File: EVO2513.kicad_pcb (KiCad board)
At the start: 8 copper layers, 110 x 69 mm, 272 parts, among them J1 1053101204, J2 1053101114, J3 10144517-043802LF, J4 1053102204, J5 1053091102, J6 1053091102, M1 78614150960, M2 78614150960, M3 78614150960, M4 78614150960, M5 78614150960, M6 78614150960, Q1 DMT6007LFGQ-7, Q10 DMT4011LFG, Q11 DMT4011LFG, Q12 DMP3007SCG-13, Q13 DMP3007SCG-13, Q14 DMP3007SCG-13, Q15 DMP3007SCG-13, Q16 IAUCN04S7L019, Q17 IAUCN04S7L028, Q18 CSD17304Q3, Q19 IAUCN04S7L019, Q20 BSS138, Q21 BSS138, Q22 BSS138, Q23 BSS138, Q24 BSS138, Q3 DMT6007LFGQ-7, Q4 DMP3007SCG-13, Q5 DMP3007SCG-13, Q6 DMT4011LFG, Q7 DMT4011LFG, Q8 DMT4011LFG, Q9 DMT4011LFG, U1 LTC1960, U10 TLV9002IDSG, U11 PCAL9714, U2 LTC4365, U5 LM51772RHAR, U6 TPS22811, U7 TPS22811, U8 TLV9002IDSG, U9 TPS22811

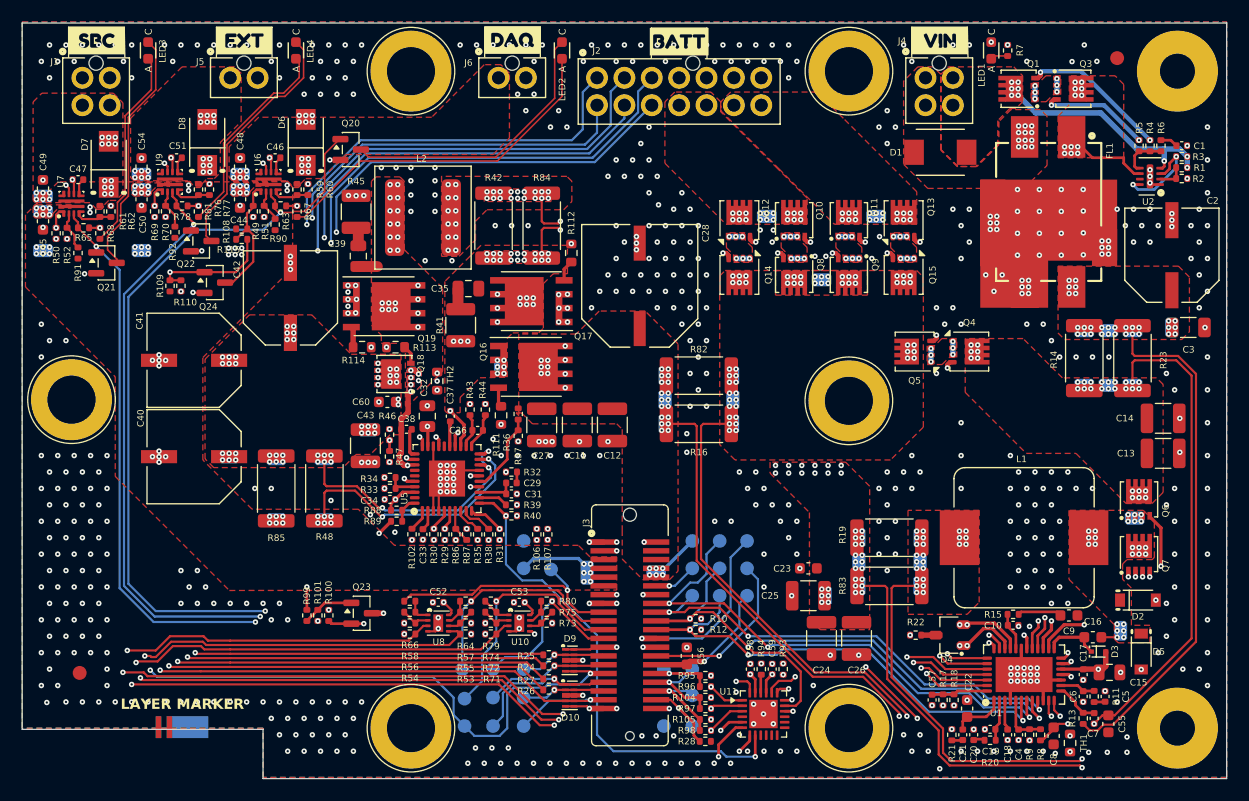
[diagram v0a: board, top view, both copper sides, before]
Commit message: Remove C55; charger layout; QC and S/N boxes
- C55 removed from the schematic and board.
- Charger-area placement and routing around U1 (C8, C7, R13, D3, DCSENSED).
- Filled QC and S/N marking boxes on the front silkscreen.

DRC: 23 violations (silk/text only), 0 unconnected, 0 parity.

Co-Authored-By: Claude Opus 5.5 <noreply@anthropic.com>
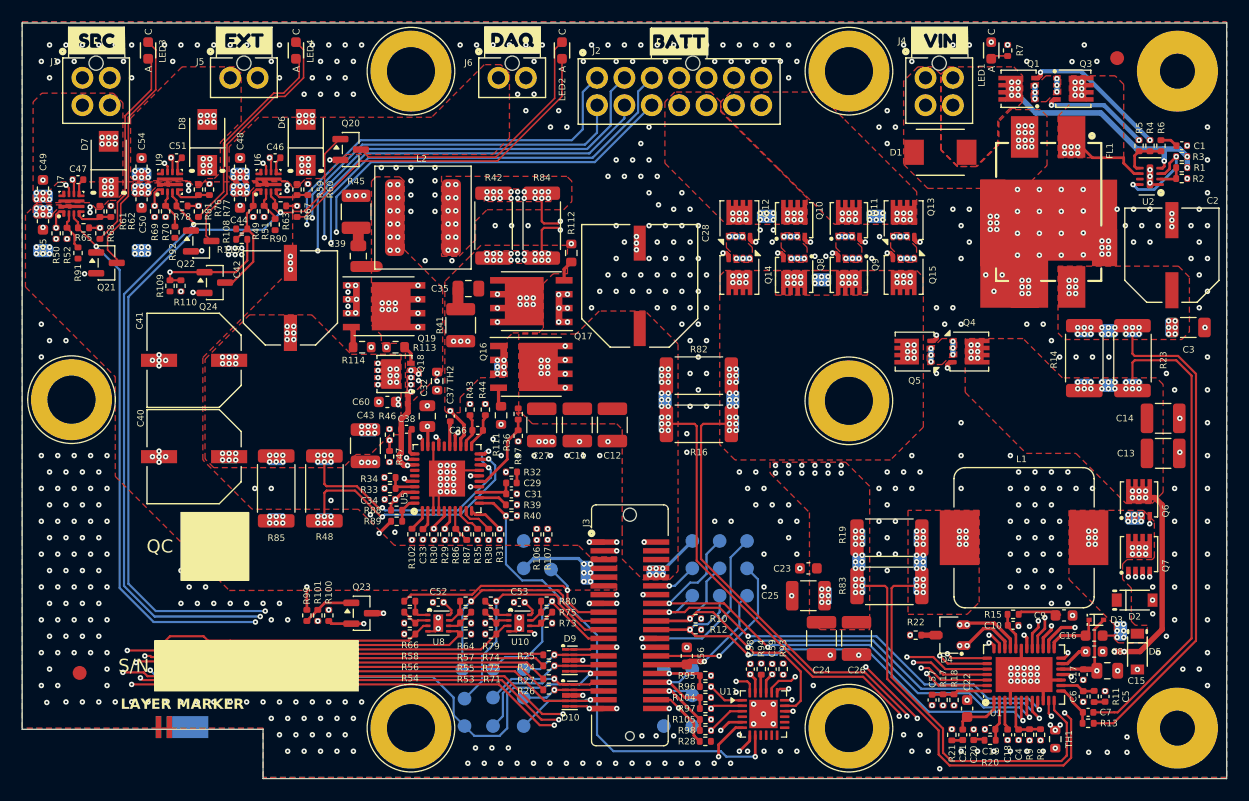
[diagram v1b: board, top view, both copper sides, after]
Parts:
- removed C55: 1uF, Capacitor_SMD:C_0603_1608Metric
- moved C8 8.54 mm to (191.4, 127.9), turned to 180 degrees
- moved D3 2.91 mm to (191.6, 125.0)
- moved TH1 1.39 mm to (187.9, 135.9)
- moved C7 0.78 mm to (190.9, 133.5), turned to 0 degrees
- moved R13 0.64 mm to (190.9, 134.5), turned to 0 degrees
- moved C9 0.45 mm to (188.7, 124.6)
- moved D5 0.35 mm to (195.4, 127.9)
- moved D2 0.30 mm to (195.1, 123.2)
- moved C15 0.25 mm to (192.6, 129.7)
- moved C16 0.19 mm to (191.4, 126.4)
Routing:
- net /DCSENSED: track 58.2 -> 80.2 mm, vias 33 -> 34
- net +5V: track 43.4 -> 46.2 mm
- net Net-(Q6-G): track 19.8 -> 17.1 mm
- net Net-(U1B-CSP): track 39.5 -> 37.0 mm, vias 26 -> 24
- net /DCFILTERED: track 76.3 -> 74.8 mm
- net /S01 External Connectors/BMSTEMP: track 53.9 -> 52.6 mm
- net Net-(Q7-G): track 15.6 -> 16.2 mm
- net GND: vias 715 -> 717
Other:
- board text added: "QC"
- board text added: "S/N"
